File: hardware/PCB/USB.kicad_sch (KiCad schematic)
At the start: 9 parts, among them CN1 USB-C, IC6 CH340G, x1 12MHZ

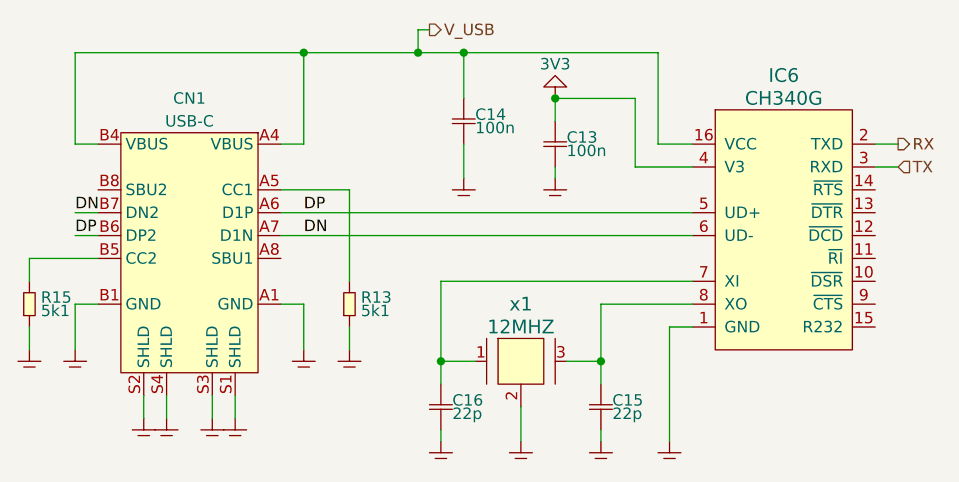
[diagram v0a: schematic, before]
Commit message: fixed the pcb being powered via ch340g
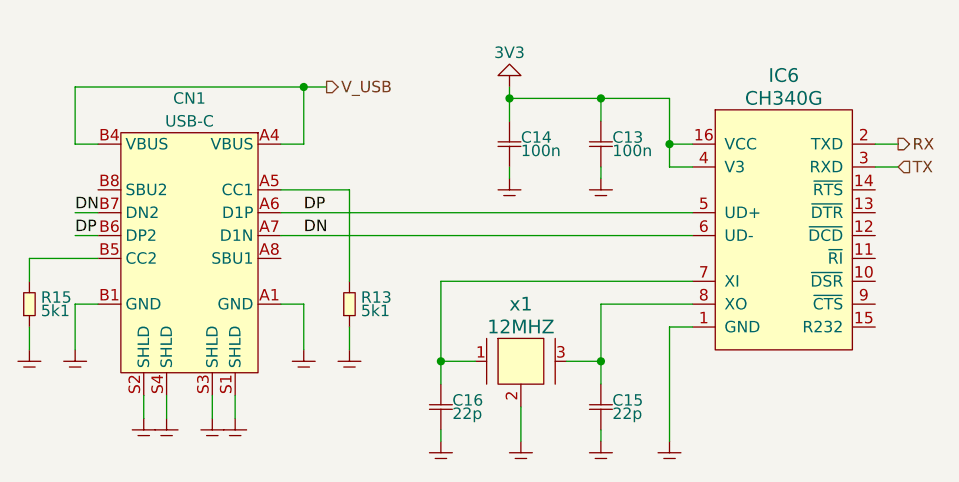
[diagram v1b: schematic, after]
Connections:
- net 3V3: now also C14.1, IC6.16 (VCC)
- net V_USB: no longer C14.1, IC6.16 (VCC)
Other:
- moved on the sheet: C13, C14
